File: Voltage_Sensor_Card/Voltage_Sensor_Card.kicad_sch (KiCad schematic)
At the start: 59 parts, among them J1 Conn_01x04, U1 ACPL-C79B, U2 MEJ1S1205SC, U3 OPA2197xD

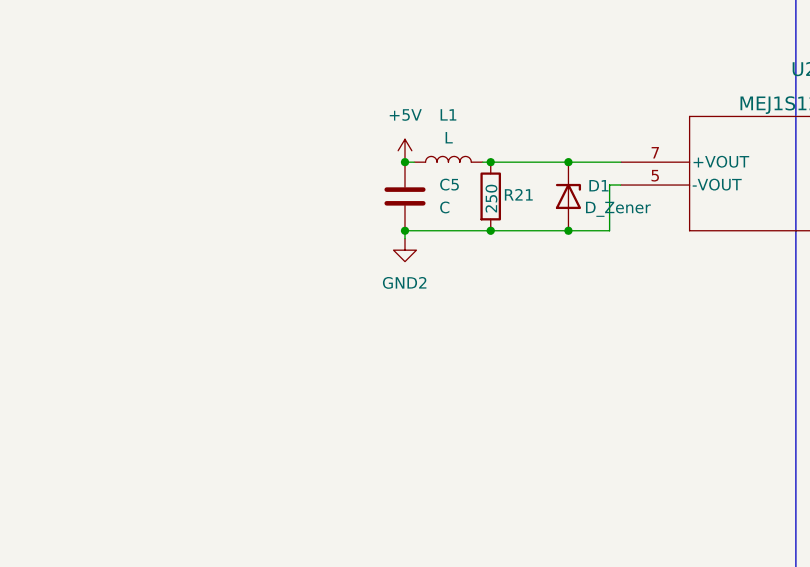
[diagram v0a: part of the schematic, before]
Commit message: Edited the layout.
Layout is not finalized yet, needs to be revised with an experienced team member.
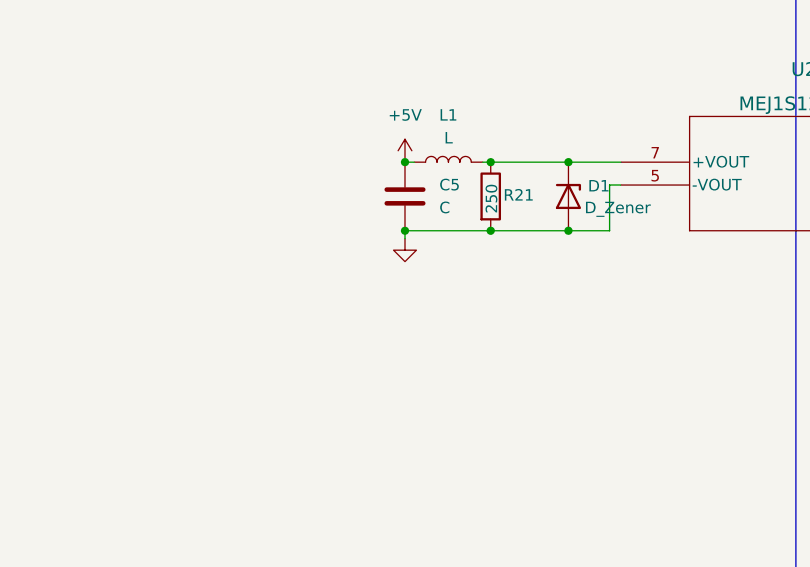
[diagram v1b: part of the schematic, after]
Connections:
- net GND1: now also C5.2, D1.2 (A), R21.2, U2.5 (-VOUT)
- net GND2: no longer C5.2, D1.2 (A), R21.2, U2.5 (-VOUT)
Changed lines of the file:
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@@
   (symbol (lib_id "power:+5VA") (at 189.484 115.57 0) (unit 1)
     (in_bom yes) (on_board yes) (fields_autoplaced)
-    (property "Reference" "#PWR?" (id 0) (at 189.484 119.38 0)
+    (property "Reference" "#PWR0101" (id 0) (at 189.484 119.38 0)
       (effects (font (size 1.27 1.27)) hide)
     )
@@
     )
     (property "Datasheet" "" (id 3) (at 157.48 25.908 0)
+      (effects (font (size 1.27 1.27)) hide)
+    )
+    (pin "1")
+  )
+  (symbol (lib_id "power:GND1") (at 104.648 105.156 0) (unit 1)
+    (in_bom yes) (on_board yes) (fields_autoplaced)
+    (property "Reference" "#PWR?" (id 0) (at 104.648 111.506 0)
+      (effects (font (size 1.27 1.27)) hide)
+    )
+    (property "Value" "" (id 1) (at 104.648 110.49 0))
+    (property "Footprint" "" (id 2) (at 104.648 105.156 0)
+      (effects (font (size 1.27 1.27)) hide)
+    )
+    (property "Datasheet" "" (id 3) (at 104.648 105.156 0)
       (effects (font (size 1.27 1.27)) hide)
     )
@@
     (pin "2")
   )
-  (symbol (lib_id "power:GND2") (at 104.648 105.156 0) (unit 1)
-    (in_bom yes) (on_board yes) (fields_autoplaced)
-    (property "Reference" "#PWR03" (id 0) (at 104.648 111.506 0)
-      (effects (font (size 1.27 1.27)) hide)
-    )
-    (property "Value" "GND2" (id 1) (at 104.648 110.109 0))
-    (property "Footprint" "" (id 2) (at 104.648 105.156 0)
-      (effects (font (size 1.27 1.27)) hide)
-    )
-    (property "Datasheet" "" (id 3) (at 104.648 105.156 0)
-      (effects (font (size 1.27 1.27)) hide)
-    )
-    (pin "1")
-  )
   (symbol (lib_id "Device:R") (at 191.516 47.879 90) (unit 1)
     (in_bom yes) (on_board yes)
@@
       (reference "#PWR02") (unit 1) (value "+5V") (footprint "")
     )
-    (path "/dbc31d27-0849-4d5b-9d29-bb94859642a9"
-      (reference "#PWR03") (unit 1) (value "GND2") (footprint "")
-    )
     (path "/19d61fad-6fc9-444f-9ff1-a7256b4bb803"
       (reference "#PWR04") (unit 1) (value "+5V") (footprint "")
@@
     )
     (path "/7d3f8118-93eb-4adf-9e49-09873711cdb2"
-      (reference "#PWR?") (unit 1) (value "+5VA") (footprint "")
+      (reference "#PWR0101") (unit 1) (value "+5VA") (footprint "")
+    )
+    (path "/9fc2c1d7-4f0e-475b-a33a-4d11684df681"
+      (reference "#PWR?") (unit 1) (value "GND1") (footprint "")
     )
     (path "/4b15b7ed-85be-46bd-8ecf-c7db11bc500e"

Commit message: Revized the layout.
Changed the orientation and placement of components, added all tracks and copper pours.
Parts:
- added C13, C14: 10u, Capacitor_SMD:C_0805_2012Metric, symbol Device:C
- added R21, R22: 10k, Resistor_SMD:R_0603_1608Metric, symbol Device:R
- J1: value Conn_01x04 -> (none); footprint Connector_PinSocket_1.00mm:PinSocket_1x04_P1.00mm_Vertical -> (none)
- renumbered C13 to C15, C14 to C16, C15 to C17, C16 to C18, C17 to C19, C18 to C20, R21 to R23, R22 to R24, R23 to R25, R24 to R26, R25 to R27, R26 to R28, R27 to R29, R28 to R30, R29 to R31, R30 to R32
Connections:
- net +15V: now also C13.1
- net -15V: now also C14.2
- net GND1: now also R21.2, R22.1
- net GND2: now also C13.2, C14.1
- net Input +: now reaches C1.1, R3.1, R4.1, TP1.1
- net at C3.1, R19.2, R20.2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: now also R21.1
- net at C4.2, R17.2, R18.2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: now also R22.2
- net Input -: now reaches C2.2, R1.1, R2.1, TP2.1
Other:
- note removed: "Input +"
- note removed: "Input -"
